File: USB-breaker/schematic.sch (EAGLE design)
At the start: 14 parts, among them K1 G6K-2P, K3 G6K-2P

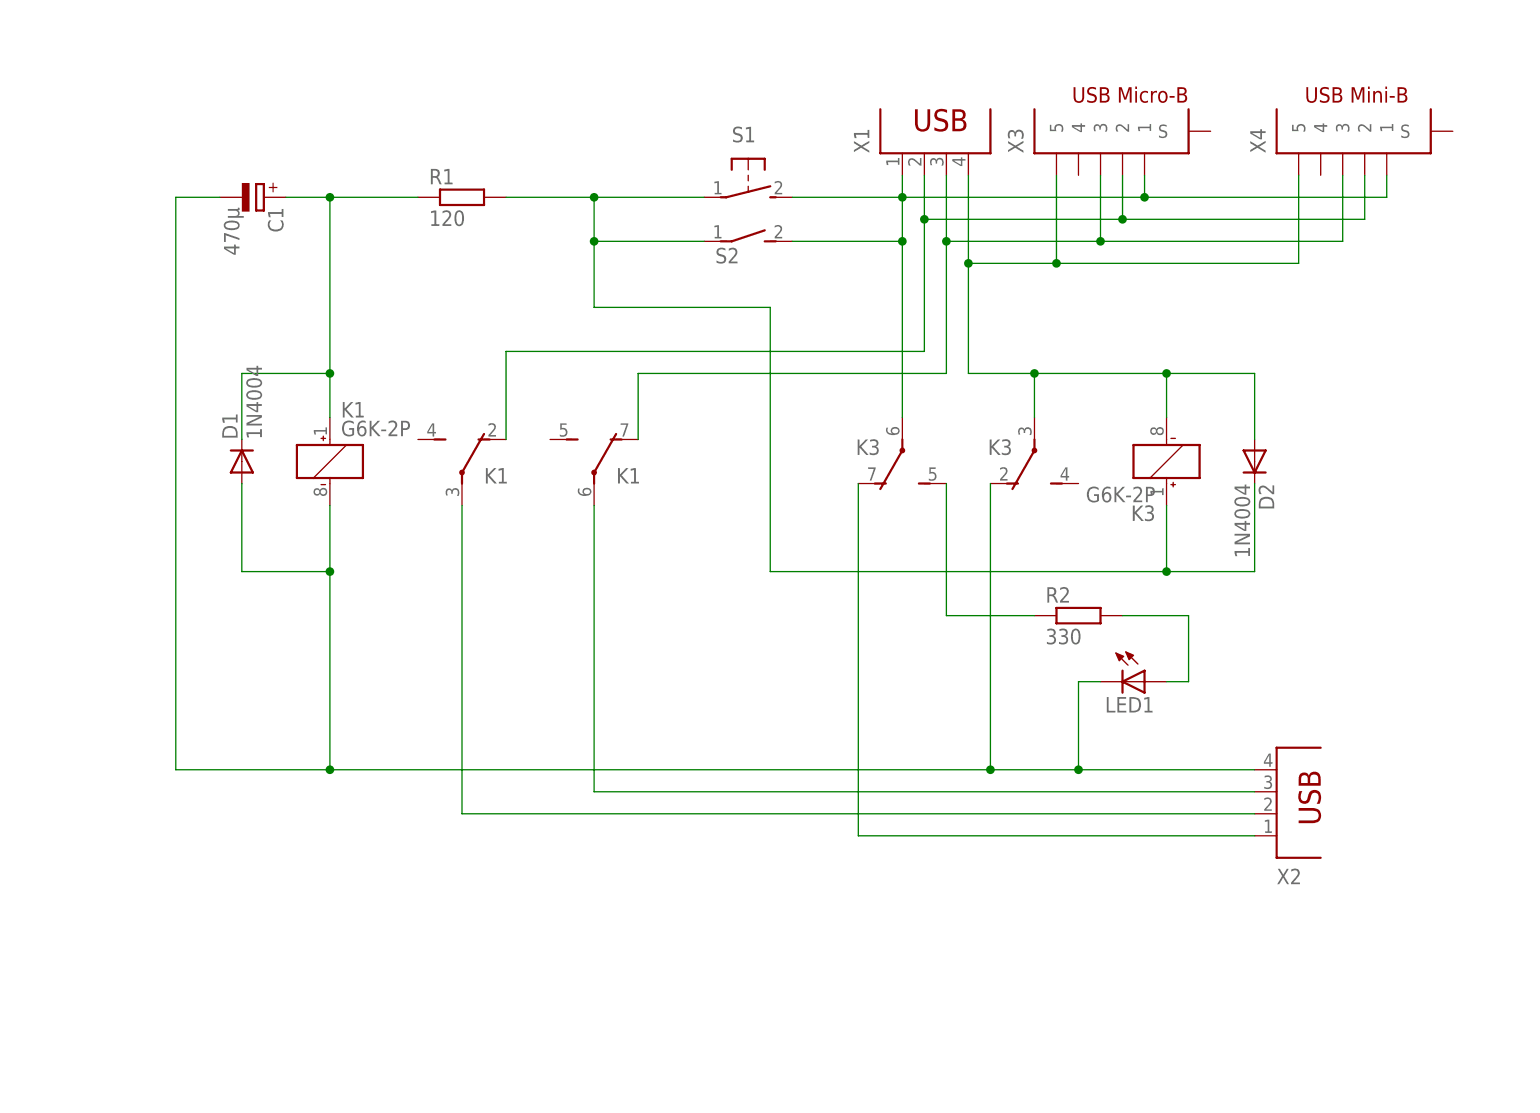
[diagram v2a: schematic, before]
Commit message: Using shielded A connectors now.
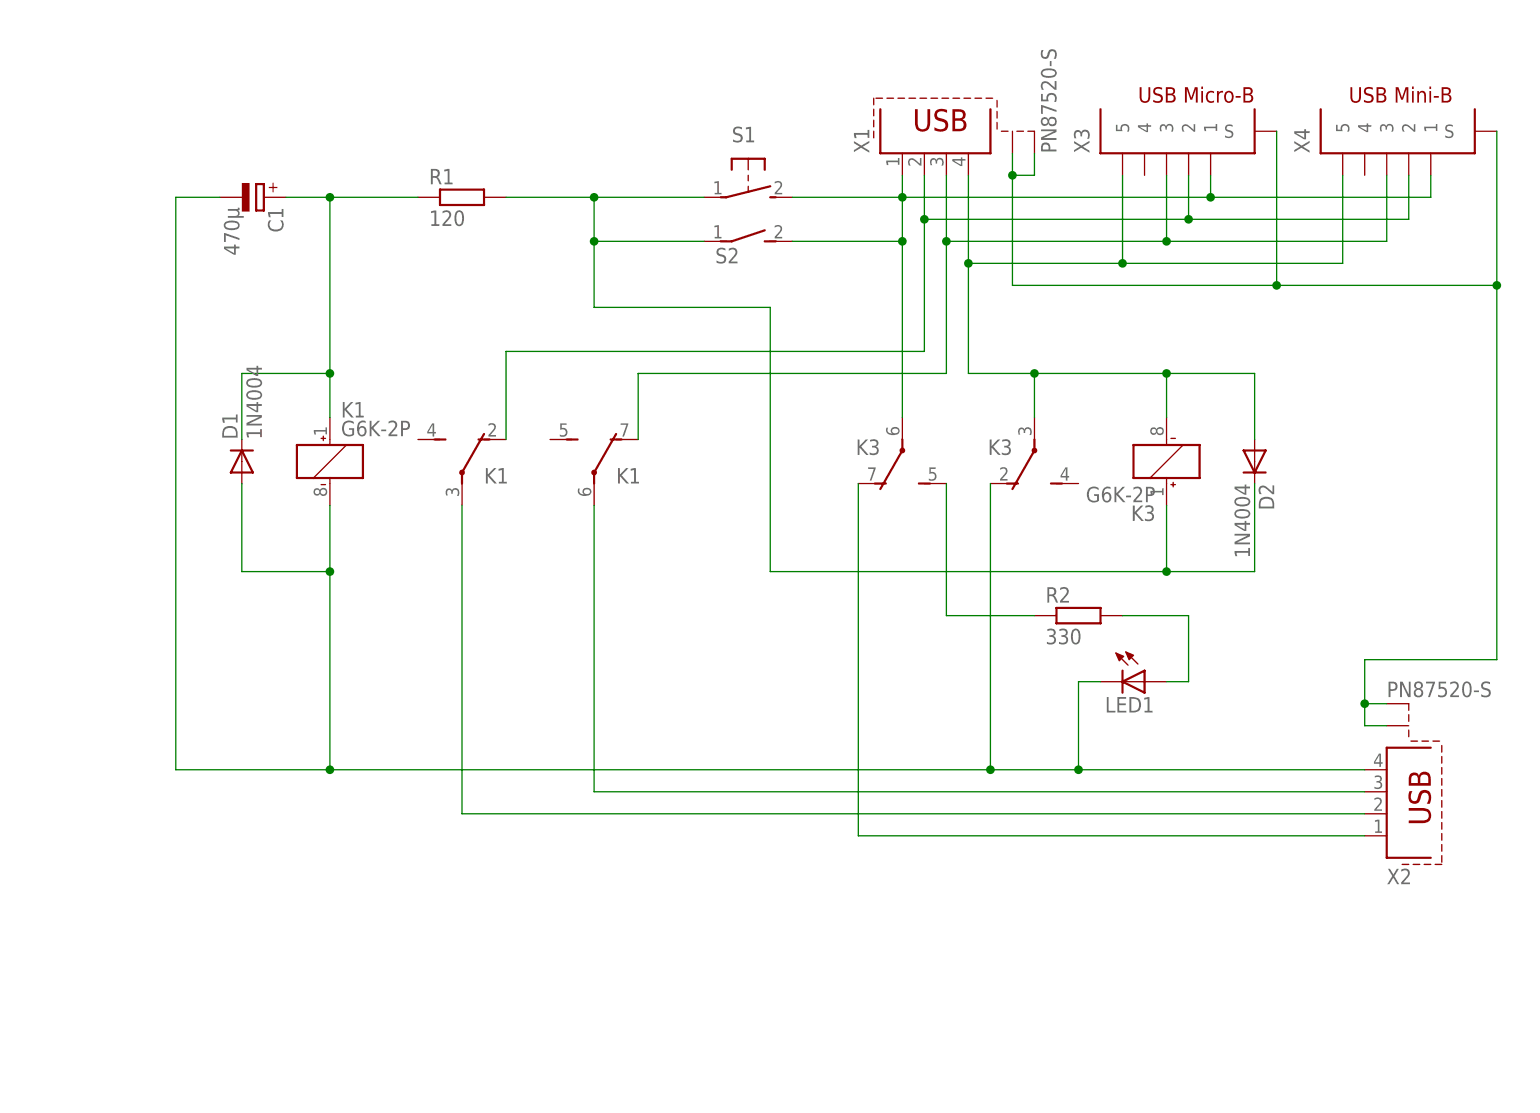
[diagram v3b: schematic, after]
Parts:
- X1, X2: value (none) -> PN87520-S; device con-berg:PN87520 -> con-berg:PN87520-S
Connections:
- new net SHIELD: X1.S1, X1.S2, X2.S1, X2.S2, X3.S, X4.S
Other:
- moved on the sheet: X3, X4
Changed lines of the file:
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@@
 <parts>
 <part name="FRAME1" library="frames" deviceset="DINA5_L" device=""/>
-<part name="X1" library="con-berg" deviceset="PN87520" device=""/>
-<part name="X2" library="con-berg" deviceset="PN87520" device=""/>
 <part name="S1" library="switch-omron" deviceset="31-XX" device=""/>
 <part name="R1" library="resistor" deviceset="R-EU_" device="0207/10" value="120"/>
@@
 <part name="X3" library="mibe" deviceset="10104110" device=""/>
 <part name="X4" library="mibe" deviceset="UX60S" device="C-MB-5ST"/>
+<part name="X2" library="con-berg" deviceset="PN87520-S" device=""/>
+<part name="X1" library="con-berg" deviceset="PN87520-S" device=""/>
 </parts>
 <sheets>
@@
 <instances>
 <instance part="FRAME1" gate="G$1" x="0" y="0"/>
-<instance part="X1" gate="G$1" x="114.3" y="114.3" rot="R90"/>
-<instance part="X2" gate="G$1" x="152.4" y="40.64" rot="MR180"/>
 <instance part="S1" gate="1" x="91.44" y="109.22" rot="R270"/>
 <instance part="R1" gate="G$1" x="58.42" y="109.22"/>
@@
 <instance part="K3" gate="2" x="124.46" y="81.28" rot="R180"/>
 <instance part="K3" gate="3" x="109.22" y="81.28" rot="R180"/>
-<instance part="X3" gate="G$1" x="137.16" y="121.92" rot="R90"/>
-<instance part="X4" gate="G$1" x="165.1" y="121.92" rot="R90"/>
+<instance part="X3" gate="G$1" x="144.78" y="121.92" rot="R90"/>
+<instance part="X4" gate="G$1" x="170.18" y="121.92" rot="R90"/>
+<instance part="X2" gate="G$1" x="165.1" y="40.64" rot="MR180"/>
+<instance part="X1" gate="G$1" x="114.3" y="114.3" rot="R90"/>
 </instances>
 <busses>
@@
 <net name="VCC-IN" class="0">
 <segment>
-<pinref part="X1" gate="G$1" pin="1"/>
 <wire x1="109.22" y1="111.76" x2="109.22" y2="109.22" width="0.1524" layer="91"/>
 <wire x1="109.22" y1="109.22" x2="109.22" y2="104.14" width="0.1524" layer="91"/>
@@
 <pinref part="K3" gate="3" pin="P"/>
 <pinref part="X3" gate="G$1" pin="1"/>
-<wire x1="109.22" y1="109.22" x2="137.16" y2="109.22" width="0.1524" layer="91"/>
-<wire x1="137.16" y1="109.22" x2="137.16" y2="111.76" width="0.1524" layer="91"/>
+<wire x1="109.22" y1="109.22" x2="144.78" y2="109.22" width="0.1524" layer="91"/>
+<wire x1="144.78" y1="109.22" x2="144.78" y2="111.76" width="0.1524" layer="91"/>
 <pinref part="X4" gate="G$1" pin="1"/>
-<wire x1="137.16" y1="109.22" x2="165.1" y2="109.22" width="0.1524" layer="91"/>
-<wire x1="165.1" y1="109.22" x2="165.1" y2="111.76" width="0.1524" layer="91"/>
-<junction x="137.16" y="109.22"/>
+<wire x1="144.78" y1="109.22" x2="170.18" y2="109.22" width="0.1524" layer="91"/>
+<wire x1="170.18" y1="109.22" x2="170.18" y2="111.76" width="0.1524" layer="91"/>
+<junction x="144.78" y="109.22"/>
+<pinref part="X1" gate="G$1" pin="1"/>
 </segment>
 </net>
 <net name="GND-IN" class="0">
 <segment>
-<pinref part="X1" gate="G$1" pin="4"/>
 <wire x1="116.84" y1="111.76" x2="116.84" y2="101.6" width="0.1524" layer="91"/>
 <wire x1="116.84" y1="101.6" x2="116.84" y2="88.9" width="0.1524" layer="91"/>
@@
 <pinref part="K3" gate="2" pin="P"/>
 <pinref part="X3" gate="G$1" pin="5"/>
-<wire x1="116.84" y1="101.6" x2="127" y2="101.6" width="0.1524" layer="91"/>
-<wire x1="127" y1="101.6" x2="127" y2="111.76" width="0.1524" layer="91"/>
+<wire x1="116.84" y1="101.6" x2="134.62" y2="101.6" width="0.1524" layer="91"/>
+<wire x1="134.62" y1="101.6" x2="134.62" y2="111.76" width="0.1524" layer="91"/>
 <junction x="116.84" y="101.6"/>
 <pinref part="X4" gate="G$1" pin="5"/>
-<wire x1="127" y1="101.6" x2="154.94" y2="101.6" width="0.1524" layer="91"/>
-<wire x1="154.94" y1="101.6" x2="154.94" y2="111.76" width="0.1524" layer="91"/>
-<junction x="127" y="101.6"/>
+<wire x1="134.62" y1="101.6" x2="160.02" y2="101.6" width="0.1524" layer="91"/>
+<wire x1="160.02" y1="101.6" x2="160.02" y2="111.76" width="0.1524" layer="91"/>
+<junction x="134.62" y="101.6"/>
+<pinref part="X1" gate="G$1" pin="4"/>
 </segment>
 </net>
@@
 <junction x="43.18" y="66.04"/>
 <pinref part="K1" gate="1" pin="-"/>
-<pinref part="X2" gate="G$1" pin="4"/>
-<wire x1="129.54" y1="43.18" x2="149.86" y2="43.18" width="0.1524" layer="91"/>
+<wire x1="129.54" y1="43.18" x2="162.56" y2="43.18" width="0.1524" layer="91"/>
 <pinref part="LED1" gate="G$1" pin="C"/>
 <wire x1="132.08" y1="53.34" x2="129.54" y2="53.34" width="0.1524" layer="91"/>
@@
 <junction x="119.38" y="43.18"/>
 <pinref part="K3" gate="2" pin="O"/>
+<pinref part="X2" gate="G$1" pin="4"/>
 </segment>
 </net>
 <net name="VCC-OUT" class="0">
 <segment>
-<pinref part="X2" gate="G$1" pin="1"/>
-<wire x1="104.14" y1="35.56" x2="149.86" y2="35.56" width="0.1524" layer="91"/>
+<wire x1="104.14" y1="35.56" x2="162.56" y2="35.56" width="0.1524" layer="91"/>
 <wire x1="104.14" y1="76.2" x2="104.14" y2="35.56" width="0.1524" layer="91"/>
 <pinref part="K3" gate="3" pin="O"/>
+<pinref part="X2" gate="G$1" pin="1"/>
 </segment>
 </net>
 <net name="D--IN" class="0">
 <segment>
-<pinref part="X1" gate="G$1" pin="2"/>
 <wire x1="111.76" y1="111.76" x2="111.76" y2="106.68" width="0.1524" layer="91"/>
 <wire x1="111.76" y1="106.68" x2="111.76" y2="91.44" width="0.1524" layer="91"/>
@@
 <wire x1="63.5" y1="91.44" x2="63.5" y2="81.28" width="0.1524" layer="91"/>
 <pinref part="X3" gate="G$1" pin="2"/>
-<wire x1="111.76" y1="106.68" x2="134.62" y2="106.68" width="0.1524" layer="91"/>
-<wire x1="134.62" y1="106.68" x2="134.62" y2="111.76" width="0.1524" layer="91"/>
+<wire x1="111.76" y1="106.68" x2="142.24" y2="106.68" width="0.1524" layer="91"/>
+<wire x1="142.24" y1="106.68" x2="142.24" y2="111.76" width="0.1524" layer="91"/>
 <junction x="111.76" y="106.68"/>
 <pinref part="X4" gate="G$1" pin="2"/>
-<wire x1="134.62" y1="106.68" x2="162.56" y2="106.68" width="0.1524" layer="91"/>
-<wire x1="162.56" y1="106.68" x2="162.56" y2="111.76" width="0.1524" layer="91"/>
-<junction x="134.62" y="106.68"/>
+<wire x1="142.24" y1="106.68" x2="167.64" y2="106.68" width="0.1524" layer="91"/>
+<wire x1="167.64" y1="106.68" x2="167.64" y2="111.76" width="0.1524" layer="91"/>
+<junction x="142.24" y="106.68"/>
+<pinref part="X1" gate="G$1" pin="2"/>
 </segment>
 </net>
 <net name="D+-IN" class="0">
 <segment>
-<pinref part="X1" gate="G$1" pin="3"/>
 <wire x1="114.3" y1="111.76" x2="114.3" y2="104.14" width="0.1524" layer="91"/>
 <wire x1="114.3" y1="104.14" x2="114.3" y2="88.9" width="0.1524" layer="91"/>
@@
 <wire x1="78.74" y1="88.9" x2="78.74" y2="81.28" width="0.1524" layer="91"/>
 <pinref part="X3" gate="G$1" pin="3"/>
-<wire x1="114.3" y1="104.14" x2="132.08" y2="104.14" width="0.1524" layer="91"/>
-<wire x1="132.08" y1="104.14" x2="132.08" y2="111.76" width="0.1524" layer="91"/>
+<wire x1="114.3" y1="104.14" x2="139.7" y2="104.14" width="0.1524" layer="91"/>
+<wire x1="139.7" y1="104.14" x2="139.7" y2="111.76" width="0.1524" layer="91"/>
 <junction x="114.3" y="104.14"/>
 <pinref part="X4" gate="G$1" pin="3"/>
-<wire x1="132.08" y1="104.14" x2="160.02" y2="104.14" width="0.1524" layer="91"/>
-<wire x1="160.02" y1="104.14" x2="160.02" y2="111.76" width="0.1524" layer="91"/>
-<junction x="132.08" y="104.14"/>
+<wire x1="139.7" y1="104.14" x2="165.1" y2="104.14" width="0.1524" layer="91"/>
+<wire x1="165.1" y1="104.14" x2="165.1" y2="111.76" width="0.1524" layer="91"/>
+<junction x="139.7" y="104.14"/>
+<pinref part="X1" gate="G$1" pin="3"/>
 </segment>
 </net>
 <net name="D+-OUT" class="0">
 <segment>
-<pinref part="X2" gate="G$1" pin="3"/>
-<wire x1="73.66" y1="40.64" x2="149.86" y2="40.64" width="0.1524" layer="91"/>
+<wire x1="73.66" y1="40.64" x2="162.56" y2="40.64" width="0.1524" layer="91"/>
 <pinref part="K1" gate="3" pin="P"/>
 <wire x1="73.66" y1="73.66" x2="73.66" y2="40.64" width="0.1524" layer="91"/>
+<pinref part="X2" gate="G$1" pin="3"/>
 </segment>
 </net>
 <net name="D--OUT" class="0">
 <segment>
-<pinref part="X2" gate="G$1" pin="2"/>
-<wire x1="58.42" y1="38.1" x2="149.86" y2="38.1" width="0.1524" layer="91"/>
+<wire x1="58.42" y1="38.1" x2="162.56" y2="38.1" width="0.1524" layer="91"/>
 <pinref part="K1" gate="2" pin="P"/>
 <wire x1="58.42" y1="73.66" x2="58.42" y2="38.1" width="0.1524" layer="91"/>
+<pinref part="X2" gate="G$1" pin="2"/>
 </segment>
 </net>
@@
 </segment>
 </net>
+<net name="SHIELD" class="0">
+<segment>
+<pinref part="X1" gate="G$1" pin="S1"/>
+<wire x1="121.92" y1="114.3" x2="121.92" y2="111.76" width="0.1524" layer="91"/>
+<pinref part="X4" gate="G$1" pin="S"/>
+<wire x1="121.92" y1="111.76" x2="121.92" y2="99.06" width="0.1524" layer="91"/>
+<wire x1="121.92" y1="99.06" x2="152.4" y2="99.06" width="0.1524" layer="91"/>
+<wire x1="152.4" y1="99.06" x2="177.8" y2="99.06" width="0.1524" layer="91"/>
+<wire x1="177.8" y1="99.06" x2="177.8" y2="116.84" width="0.1524" layer="91"/>
+<pinref part="X3" gate="G$1" pin="S"/>
+<wire x1="152.4" y1="116.84" x2="152.4" y2="99.06" width="0.1524" layer="91"/>
+<junction x="152.4" y="99.06"/>
+<pinref part="X1" gate="G$1" pin="S2"/>
+<wire x1="124.46" y1="114.3" x2="124.46" y2="111.76" width="0.1524" layer="91"/>
+<wire x1="124.46" y1="111.76" x2="121.92" y2="111.76" width="0.1524" layer="91"/>
+<junction x="121.92" y="111.76"/>
+<wire x1="177.8" y1="99.06" x2="177.8" y2="55.88" width="0.1524" layer="91"/>
+<junction x="177.8" y="99.06"/>
+<wire x1="177.8" y1="55.88" x2="162.56" y2="55.88" width="0.1524" layer="91"/>
+<wire x1="162.56" y1="55.88" x2="162.56" y2="50.8" width="0.1524" layer="91"/>
+<pinref part="X2" gate="G$1" pin="S2"/>
+<wire x1="162.56" y1="50.8" x2="165.1" y2="50.8" width="0.1524" layer="91"/>
+<wire x1="162.56" y1="50.8" x2="162.56" y2="48.26" width="0.1524" layer="91"/>
+<junction x="162.56" y="50.8"/>
+<pinref part="X2" gate="G$1" pin="S1"/>
+<wire x1="162.56" y1="48.26" x2="165.1" y2="48.26" width="0.1524" layer="91"/>
+</segment>
+</net>

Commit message: Using a shrouded PIN header for the interface elements (LED, button & switch)
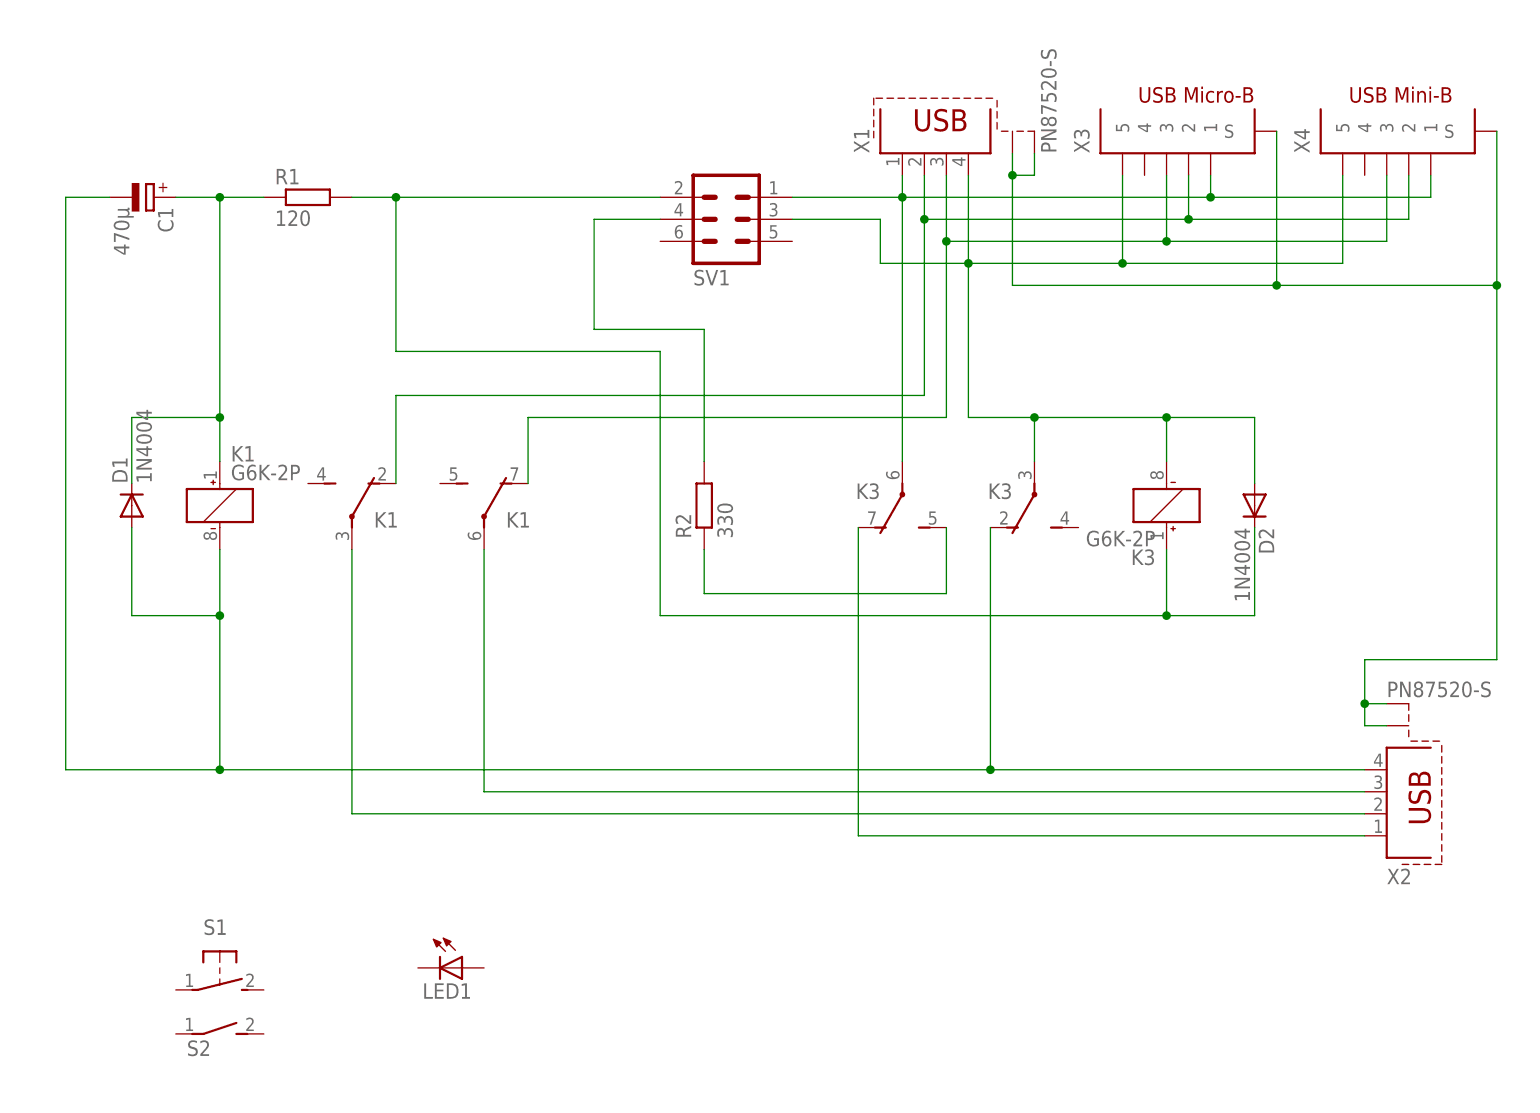
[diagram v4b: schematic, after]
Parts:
- added SV1: (no value), con-harting-ml:ML6
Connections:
- net N$7 renamed VCC_LED
- removed net N$9: LED1.A, R2.2
- new net LED: R2.2, SV1.4
- net ENABLE: now also SV1.2; no longer S1.P, S2.1
- net GND-IN: now also SV1.3
- net GND-OUT: no longer LED1.C
- net VCC-IN: now also SV1.1; no longer S1.S, S2.2
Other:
- moved on the sheet: C1, D1, D2, K1, K3, LED1, R1, R2, S1, S2
